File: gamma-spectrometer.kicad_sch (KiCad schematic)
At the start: 36 parts, among them T1 T1-1T-KK81, U1 Pico 2, U2 MAX1422ECM+D, U3 TLV3201AIDBVR, U4 MAX5026EUT_T, U6 MCP41050-I_SN

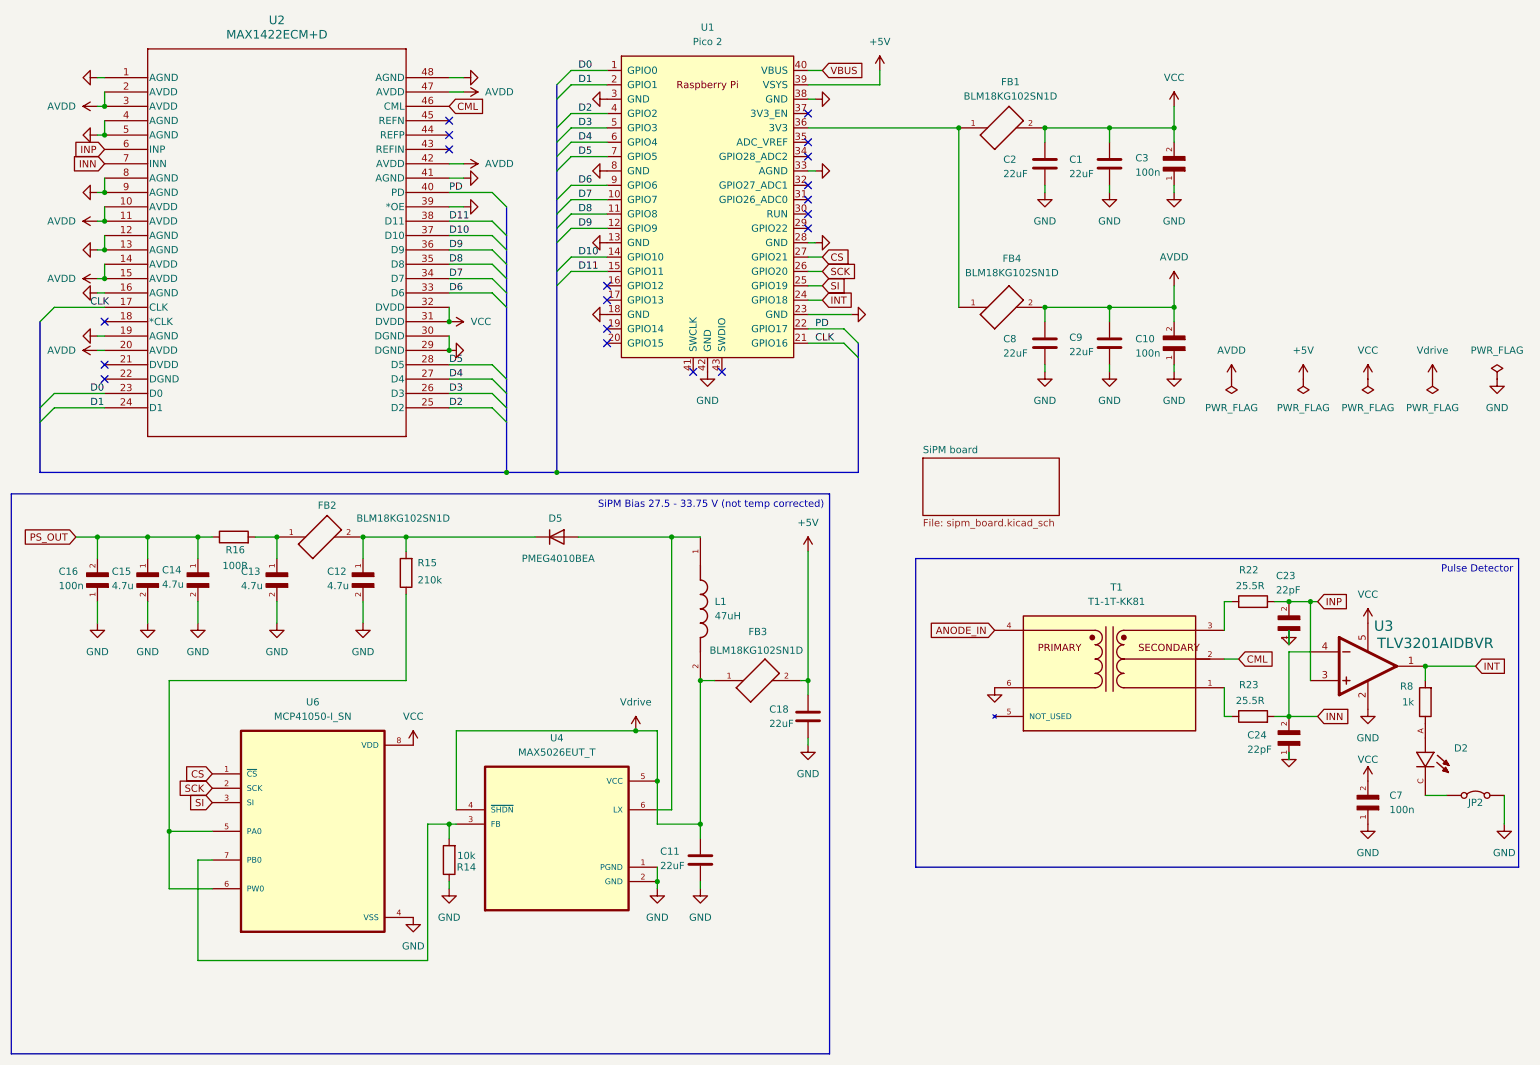
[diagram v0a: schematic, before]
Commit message: ADC capacitors
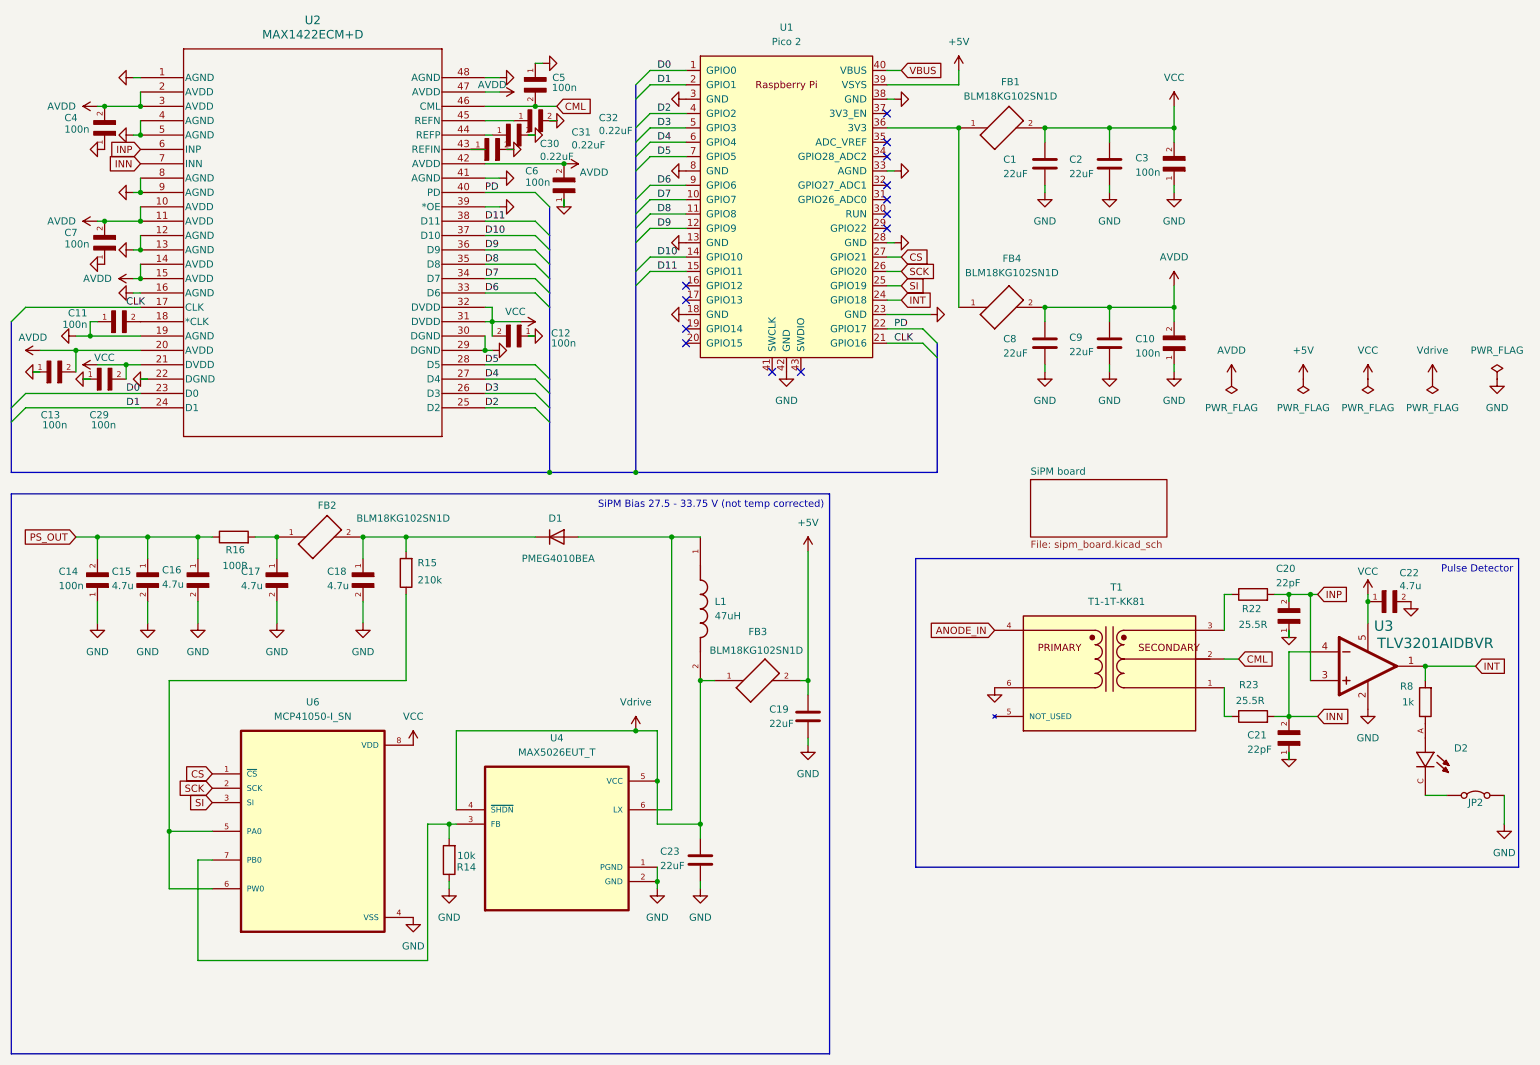
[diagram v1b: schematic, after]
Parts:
- added C11, C12, C13, C29, C4, C5, C6: 100n, CL10B104KC8NNNC:CAPC1608X90N, symbol CL10B104KC8NNNC:CL10B104KC8NNNC
- added C22: 4.7u, CL21A475KBQNNNE:CAPC2012X140N, symbol CL21A475KBQNNNE:CL21A475KBQNNNE
- added C30, C31, C32: 0.22uF, C1608JB1H224K080AB:CAPC1608X90N, symbol C1608JB1H224K080AB:C1608JB1H224K080AB
- renumbered C2 to C1, C16 to C14, C14 to C16, C13 to C17, C12 to C18, C18 to C19, C1 to C2, C23 to C20, C24 to C21, C11 to C23, D5 to D1
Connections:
- net AVDD: now also C7.2, C13.2, C4.2, C6.2
- net CML: now also C5.2
- net GND: now also U2.22 (DGND), C11.1, C12.1, C13.1, C22.2, C29.1, C30.2, C31.2, C32.2, C4.1, C5.1, C6.1
- net VCC: now also U2.21 (DVDD), C12.2, C22.1, C29.2; no longer C7.2
- net at U2.18 (*CLK): now also C11.2
- net at U2.43 (REFIN): now also C30.1
- net at U2.44 (REFP): now also C31.1
- net at U2.45 (REFN): now also C32.1
- no-connect marks 19 -> 13
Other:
- moved on the sheet: C20, R22, U1, U2

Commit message: Package update
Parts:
- U2: MP (none) -> MAX1422ECM+D; Package (none) -> LQFP-48
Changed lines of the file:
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@@
+			)
+		)
+		(property "MP" "MAX1422ECM+D"
+			(at 39.37 24.13 0)
+			(effects
+				(font
+					(size 1.27 1.27)
+				)
+				(hide yes)
+			)
+		)
+		(property "Package" "LQFP-48"
+			(at 39.37 24.13 0)
+			(effects
+				(font
+					(size 1.27 1.27)
+				)
+				(hide yes)
 			)
 		)

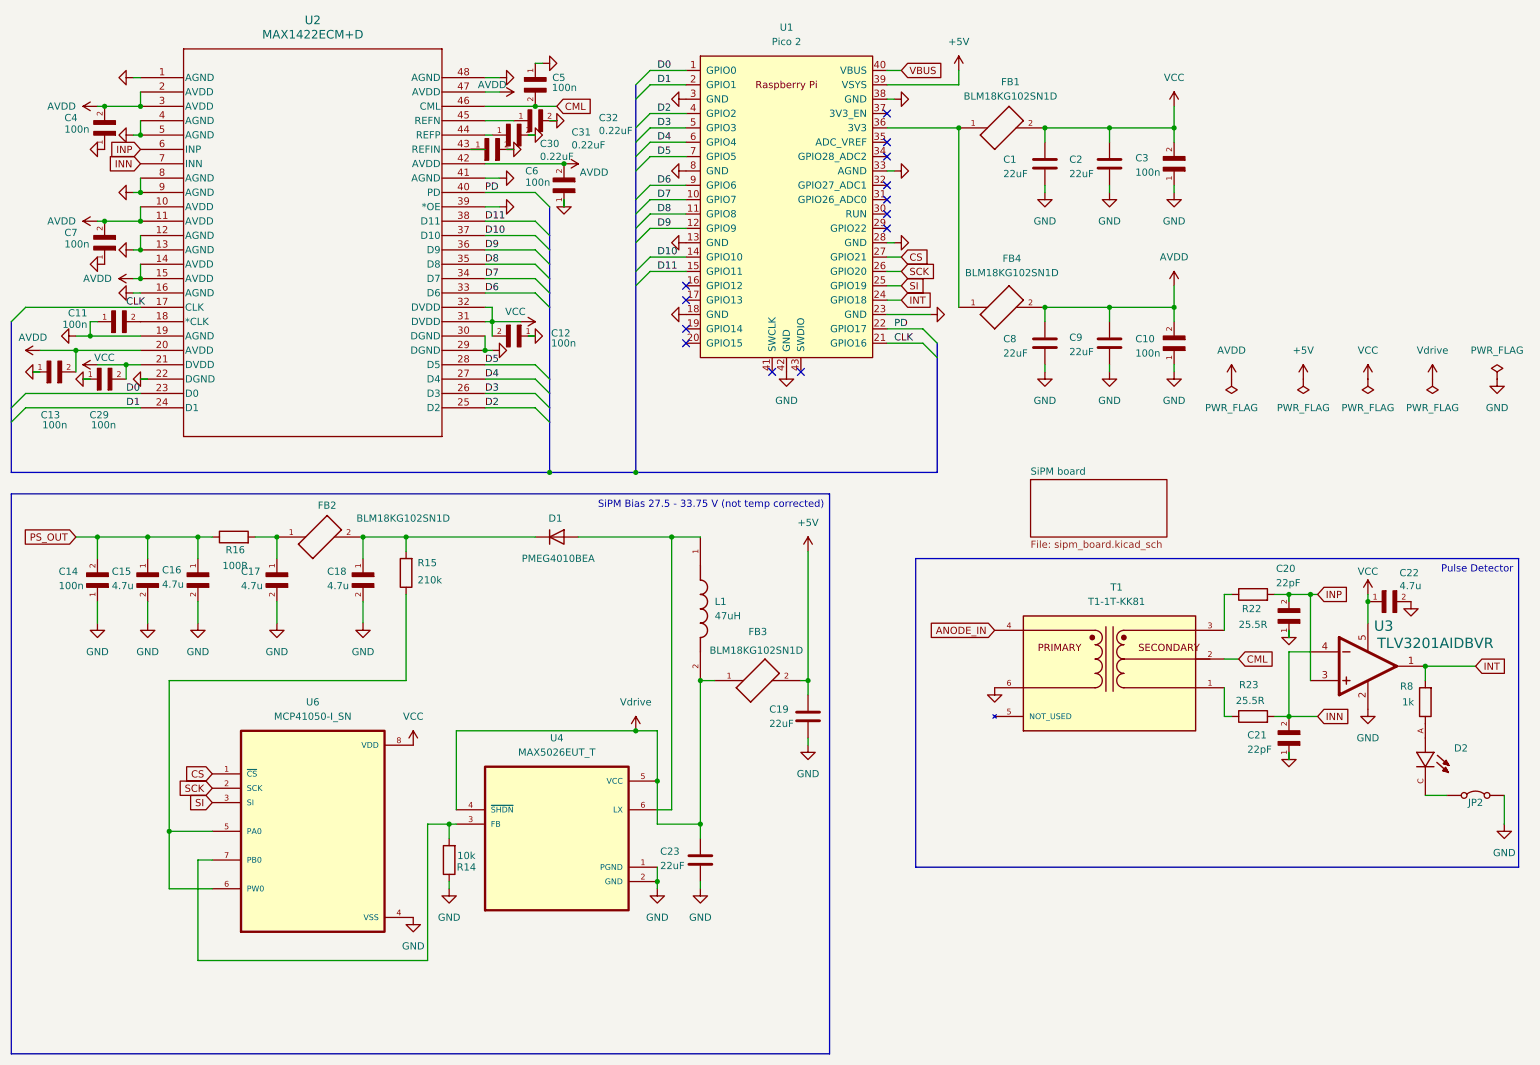
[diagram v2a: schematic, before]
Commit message: Digital potentiometer improvement
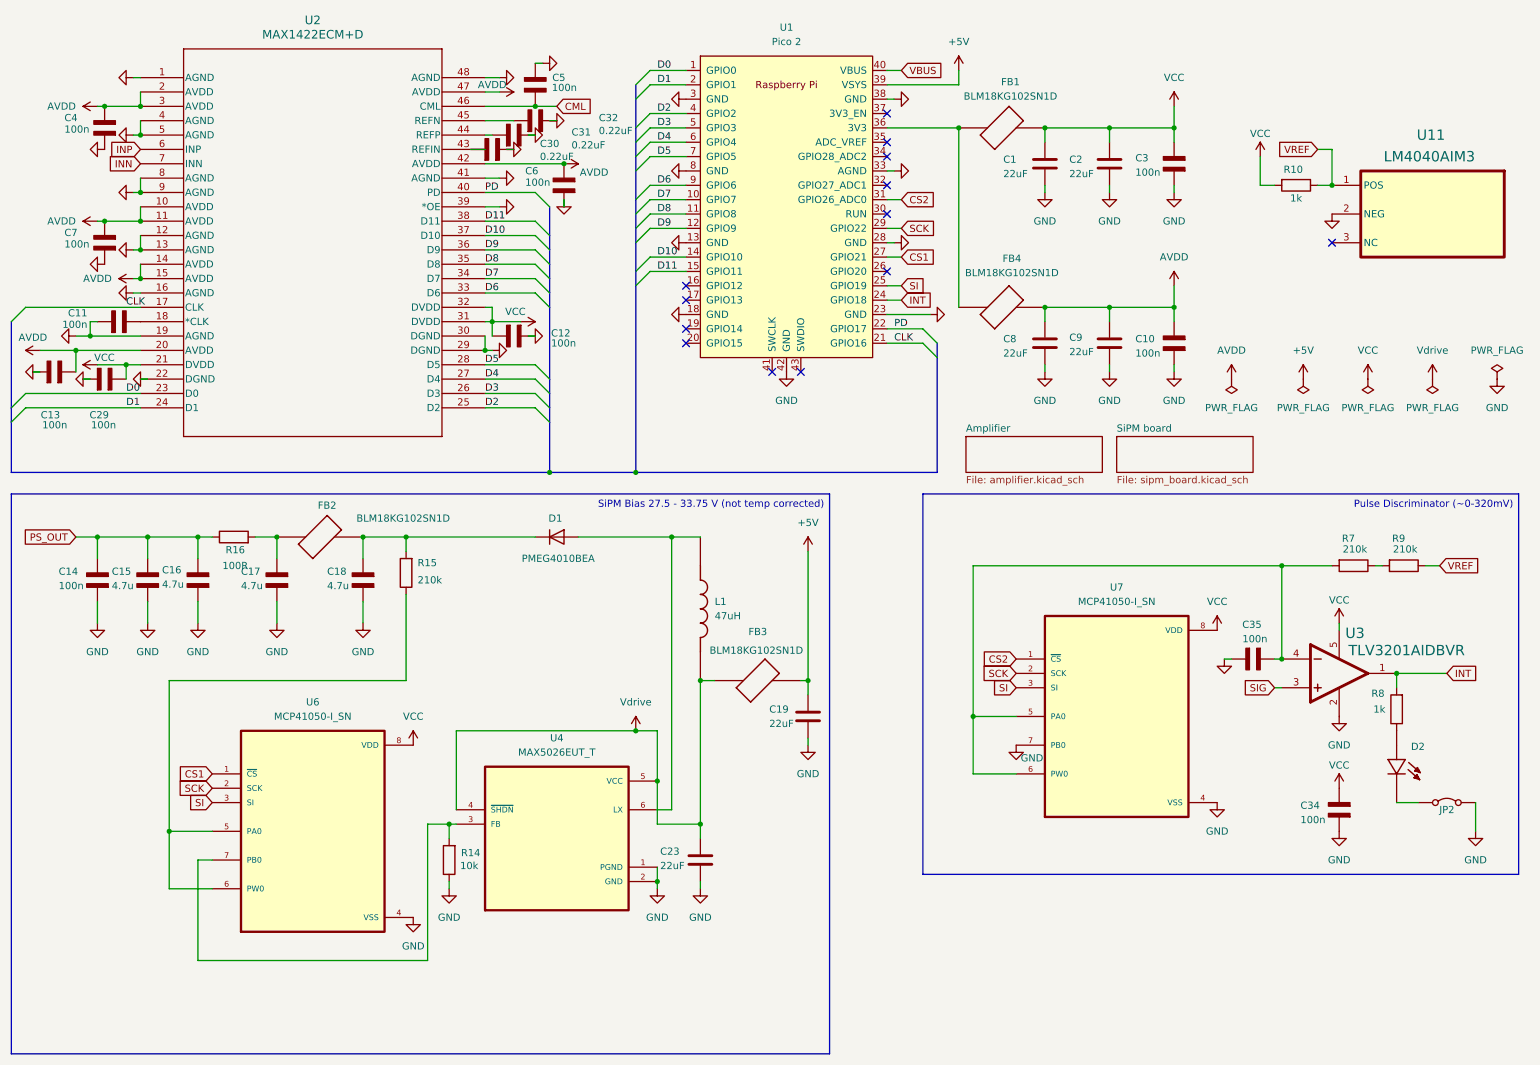
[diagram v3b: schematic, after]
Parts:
- removed C20, C21: 22pF, ECJ-1VC1H220J:CAPC1608X90N, symbol ECHU1C471JX5:ECHU1C471JX5
- removed C22: 4.7u, CL21A475KBQNNNE:CAPC2012X140N, symbol CL21A475KBQNNNE:CL21A475KBQNNNE
- removed R22, R23: 25.5R, ERJ3EKF25R5V:RES_ERJ3EKF25R5V, symbol Device:R
- removed T1: T1-1T-KK81, T1-1T-KK81:XFMR_T1-1T-KK81_, symbol T1-1T-KK81:T1-1T-KK81_
- added C34, C35: 100n, CL10B104KC8NNNC:CAPC1608X90N, symbol CL10B104KC8NNNC:CL10B104KC8NNNC
- added R10: 1k, ERJ3EKF1001V:RES_ERJ3EKF1001V, symbol Device:R
- added R7, R9: 210k, ERJ3EKF2103V:RES_ERJ3EKF2103V, symbol Device:R
- added U11: LM4040AIM3, LM4040AIM3-3_0-T:SOT95P237X112-3N, symbol LM4040AIM3-3_0-T:LM4040AIM3-3_0-T
- added U7: MCP41050-I_SN, MCP41050-I_SN:SOIC127P600X175-8N, symbol MCP41050-I_SN:MCP41050-I_SN
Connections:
- net GND: now also C34.1, C35.2, U11.2 (NEG), U7.4 (VSS), U7.7 (PB0)
- net INN: no longer U3.4 (IN-)
- net INP: no longer U3.3 (IN+)
- net SCK: now also U1.29 (GPIO22), U7.2 (SCK); no longer U1.26 (GPIO20)
- net SI: now also U7.3 (SI)
- net VCC: now also C34.2, R10.2, U7.8 (VDD)
- net CS2: now reaches U1.31 (GPIO26_ADC0)
- net CS2: now also U7.1 (~{CS})
- net CS renamed CS1
- new net: R7.1, R9.2
- new net: C35.1, R7.2, U3.4 (IN-), U7.5 (PA0), U7.6 (PW0)
- new net SIG: U3.3 (IN+)
- new net VREF: R10.1, R9.1, U11.1 (POS)
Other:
- added sheet Amplifier (amplifier.kicad_sch)
- moved on the sheet: JP2, R8, U3

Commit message: 3d models update
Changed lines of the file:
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@@
 	(title_block
 		(title "Gamma Spectrometer")
-		(date "2025-09-06")
-		(rev "0.2.1")
+		(date "2025-09-07")
+		(rev "0.2.3")
 		(company "Vadym Vikulin")
 	)
@@
 				(size 1.27 1.27)
 			)
-			(justify right top)
+			(justify left top)
 		)
 	)
@@
 		(stroke
 			(width 0)
-			(type default)
+			(type solid)
 		)
 		(fill
@@
 				(size 1.27 1.27)
 			)
-			(justify right top)
+			(justify left top)
 		)
 	)
